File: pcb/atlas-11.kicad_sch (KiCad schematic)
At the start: 5 parts, among them J1 USB_C_Receptacle, J2 DCJ-11 SBC Expansion Bus, J3 Micro_SD_Card_Det2, U1 RP2350B-QFN80, U2 TPS22810DBVR

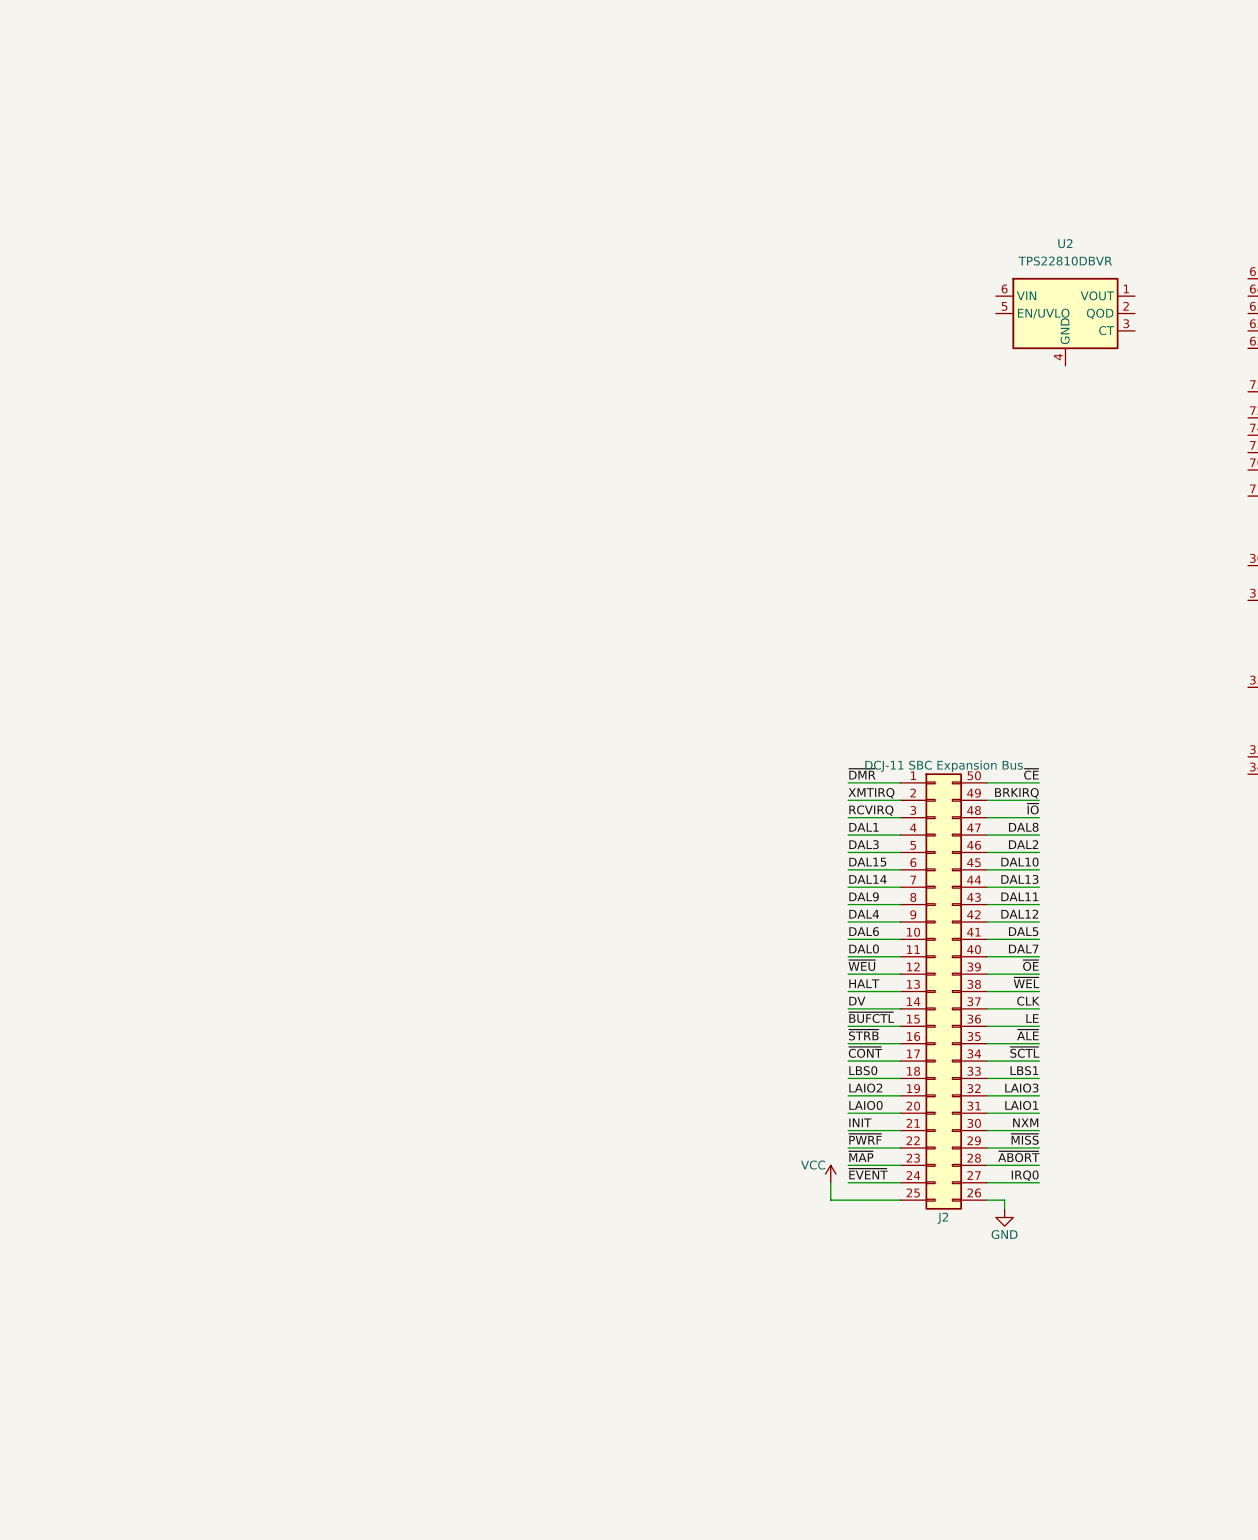
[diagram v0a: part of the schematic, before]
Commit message: add more sections from rp2350 minimal example
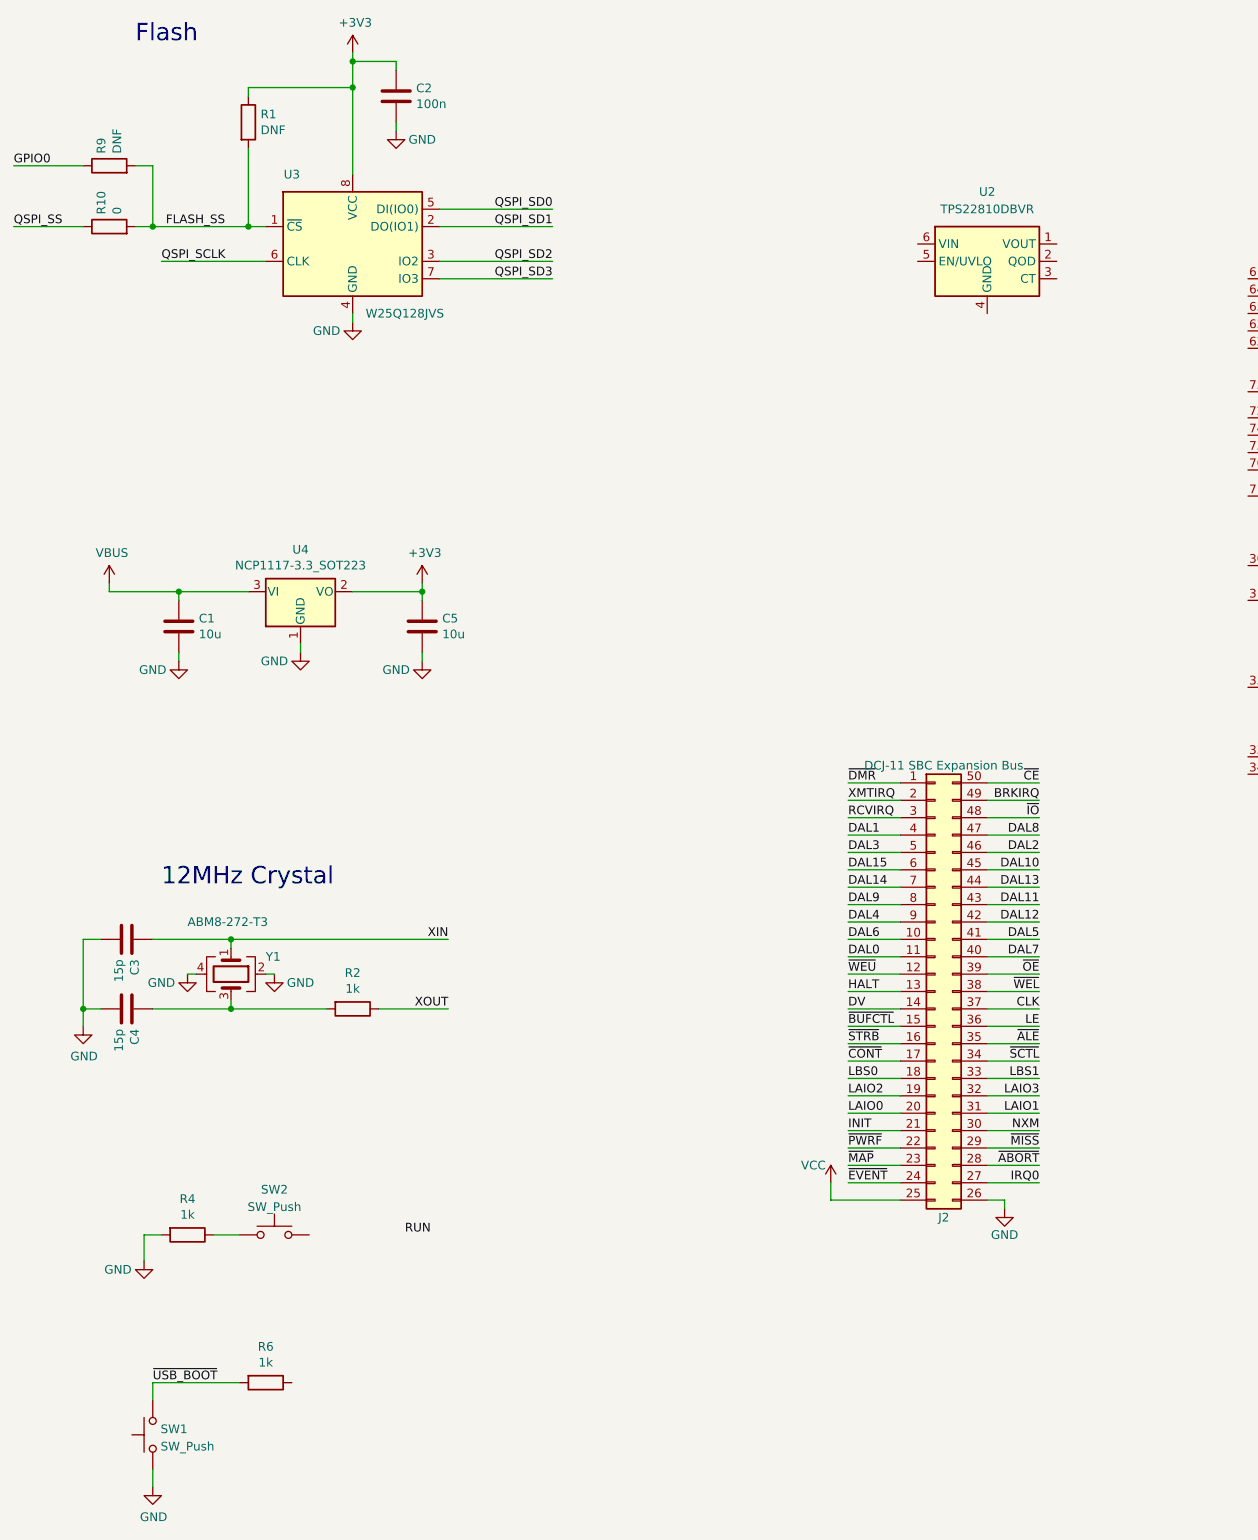
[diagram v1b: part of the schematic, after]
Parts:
- added C1, C5: 10u, Capacitor_SMD:C_0805_2012Metric, symbol Device:C
- added C2: 100n, Capacitor_SMD:C_0402_1005Metric, symbol Device:C
- added C3, C4: 15p, Capacitor_SMD:C_0402_1005Metric, symbol Device:C
- added R1, R9: DNF, Resistor_SMD:R_0402_1005Metric, symbol Device:R
- added R10: 0, Resistor_SMD:R_0402_1005Metric, symbol Device:R
- added R2, R4, R6: 1k, Resistor_SMD:R_0402_1005Metric, symbol Device:R
- added SW1, SW2: SW_Push, Button_Switch_SMD:SW_Push_1P1T_NO_Vertical_Wuerth_434133025816, symbol Switch:SW_Push
- added U3: W25Q128JVS, Package_SO:SOIC-8_5.23x5.23mm_P1.27mm, symbol Memory_Flash:W25Q128JVS
- added U4: NCP1117-3.3_SOT223, Package_TO_SOT_SMD:SOT-223-3_TabPin2, symbol Regulator_Linear:NCP1117-3.3_SOT223
- added Y1: ABM8-272-T3, Crystal:Crystal_SMD_3225-4Pin_3.2x2.5mm, symbol Device:Crystal_GND24
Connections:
- net GND: now also C1.2, C2.2, C3.2, C4.2, C5.2, R4.2, SW1.1, U3.4 (GND), U4.1 (GND), Y1.2, Y1.4
- new net: R4.1, SW2.1
- new net: C4.1, R2.2, Y1.3
- new net +3V3: C2.1, C5.1, R1.1, U3.8 (VCC), U4.2 (VO)
- new net FLASH_SS: R1.2, R10.2, R9.2, U3.1 (~{CS})
- new net GPIO0: R9.1
- new net QSPI_SCLK: U3.6 (CLK)
- new net QSPI_SD0: U3.5 (DI(IO0))
- new net QSPI_SD1: U3.2 (DO(IO1))
- new net QSPI_SD2: U3.3 (IO2)
- new net QSPI_SD3: U3.7 (IO3)
- new net QSPI_SS: R10.1
- new net VBUS: C1.1, U4.3 (VI)
- new net XIN: C3.1, Y1.1
- new net XOUT: R2.1
- new net ~{USB_BOOT}: R6.2, SW1.2
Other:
- note added: "12MHz Crystal"
- note added: "Flash"
- moved on the sheet: U2

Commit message: schematics & pcb work
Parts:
- removed R1, R9: DNF, Resistor_SMD:R_0402_1005Metric, symbol Device:R
- removed R10: 0, Resistor_SMD:R_0402_1005Metric, symbol Device:R
- added C10, C9: 4.7u, Capacitor_SMD:C_0402_1005Metric, symbol Device:C
- added C11, C12, C13, C14, C15, C16, C17, C18, C19, C20, C8: 100n, Capacitor_SMD:C_0402_1005Metric, symbol Device:C
- added C6, C7: 4.7u, RP2350_60QFN_minimal:C_0402_1005Metric_small_pads, symbol Device:C
- added J4: DCJ-11 SBC Bus Probe Interface, Library:DCJ-11 SBC Expansion Port Debug Header, symbol Connector_Generic:Conn_02x25_Counter_Clockwise
- added L1: 3.3u, RP2350_60QFN_minimal:L_pol_2016, symbol Device:L
- added R5: 33, Resistor_SMD:R_0402_1005Metric, symbol Device:R
- added R7, R8: 27, Resistor_SMD:R_0402_1005Metric, symbol Device:R
- J1: value USB_C_Receptacle -> USB
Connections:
- net FLASH_SS is gone; now on net QSPI_SS: U3.1 (~{CS})
- net VCC is gone; now on net SBC_POWER: J2.25 (Pin_25)
- net +3V3: now also U1.15 (IOVDD), U1.24 (IOVDD), U1.29 (IOVDD), U1.41 (IOVDD), U1.5 (IOVDD), U1.50 (IOVDD), U1.59 (ADC_AVDD), U1.60 (IOVDD), U1.64 (VREG_VIN), U1.68 (USB_OTP_VDD), U1.69 (QSPI_IOVDD), U1.76 (IOVDD), C12.1, C13.1, C14.1, C15.1, C16.1, C17.1, C18.1, C6.1, R5.1
- net BRKIRQ: now also J4.49 (Pin_49)
- net CLK: now also J4.37 (Pin_37)
- net DAL0: now also U1.2 (GPIO5), J4.11 (Pin_11)
- net DAL1: now also U1.3 (GPIO6), J4.4 (Pin_4)
- net DAL10: now also U1.14 (GPIO15), J4.45 (Pin_45)
- net DAL11: now also U1.16 (GPIO16), J4.43 (Pin_43)
- net DAL12: now also U1.17 (GPIO17), J4.42 (Pin_42)
- net DAL13: now also U1.18 (GPIO18), J4.44 (Pin_44)
- net DAL14: now also U1.19 (GPIO19), J4.7 (Pin_7)
- net DAL15: now also U1.20 (GPIO20), J4.6 (Pin_6)
- net DAL2: now also U1.4 (GPIO7), J4.46 (Pin_46)
- net DAL3: now also U1.6 (GPIO8), J4.5 (Pin_5)
- net DAL4: now also U1.7 (GPIO9), J4.9 (Pin_9)
- net DAL5: now also U1.8 (GPIO10), J4.41 (Pin_41)
- net DAL6: now also U1.9 (GPIO11), J4.10 (Pin_10)
- net DAL7: now also U1.11 (GPIO12), J4.40 (Pin_40)
- net DAL8: now also U1.12 (GPIO13), J4.47 (Pin_47)
- net DAL9: now also U1.13 (GPIO14), J4.8 (Pin_8)
- net DV: now also J4.14 (Pin_14)
- net GND: now also U1.62 (VREG_PGND), U2.4 (GND), U2.7 (GND), C10.2, C11.2, C12.2, C13.2, C14.2, C15.2, C16.2, C17.2, C18.2, C19.2, C20.2, C6.2, C7.2, C8.2, C9.2, J4.26 (Pin_26)
- net HALT: now also J4.13 (Pin_13)
- net INIT: now also J4.21 (Pin_21)
- net IRQ0: now also J4.27 (Pin_27)
- net LAIO0: now also J4.20 (Pin_20)
- net LAIO1: now also J4.31 (Pin_31)
- net LAIO2: now also J4.19 (Pin_19)
- net LAIO3: now also J4.32 (Pin_32)
- net LBS0: now also J4.18 (Pin_18)
- net LBS1: now also J4.33 (Pin_33)
- net LE: now also J4.36 (Pin_36)
- net NXM: now also J4.30 (Pin_30)
- net QSPI_SCLK: now also U1.71 (QSPI_SCLK)
- net QSPI_SD0: now also U1.72 (QSPI_SD0)
- net QSPI_SD1: now also U1.74 (QSPI_SD1)
- net QSPI_SD2: now also U1.73 (QSPI_SD2)
- net QSPI_SD3: now also U1.70 (QSPI_SD3)
- net QSPI_SS: now also R6.1, U1.75 (QSPI_SS)
- net RCVIRQ: now also J4.3 (Pin_3)
- net VBUS: now also U2.6 (VIN), C20.1
- net XIN: now also U1.30 (XIN)
- net XMTIRQ: now also J4.2 (Pin_2)
- net XOUT: now also U1.31 (XOUT)
- net ~{ABORT}: now also J4.28 (Pin_28)
- net ~{ALE}: now also J4.35 (Pin_35)
- net ~{BUFCTL}: now also J4.15 (Pin_15)
- net ~{CE}: now also J4.50 (Pin_50)
- net ~{CONT}: now also J4.17 (Pin_17)
- net ~{DMR}: now also J4.1 (Pin_1)
- net ~{EVENT}: now also J4.24 (Pin_24)
- net ~{IO}: now also J4.48 (Pin_48)
- net ~{MAP}: now also J4.23 (Pin_23)
- net ~{MISS}: now also J4.29 (Pin_29)
- net ~{OE}: now also J4.39 (Pin_39)
- net ~{PWRF}: now also J4.22 (Pin_22)
- net ~{SCTL}: now also J4.34 (Pin_34)
- net ~{STRB}: now also J4.16 (Pin_16)
- net ~{WEL}: now also J4.38 (Pin_38)
- net ~{WEU}: now also J4.12 (Pin_12)
- net at SW2.2: now also U1.35 (RUN)
- net SBC_POWER: now reaches U2.1 (VOUT)
- net SBC_POWER: now also C19.1, J4.25 (Pin_25)
- net SBC_ON: now reaches U2.5 (EN/UVLO)
- net SBC_ON: now also U1.79 (GPIO2)
- net +1V1: now reaches U1.10 (DVDD)
- net +1V1: now also U1.32 (DVDD), U1.51 (DVDD), U1.65 (VREG_FB), C10.1, C11.1, C7.1, C8.1, L1.1
- net VREG_AVDD: now reaches U1.61 (VREG_AVDD)
- net VREG_AVDD: now also C9.1, R5.2
- net VREG_LX: now reaches U1.63 (VREG_LX)
- net VREG_LX: now also L1.2
- net at U1.66 (USB_DM): now also R8.2
- net at U1.67 (USB_DP): now also R7.2
- new net USB_D+: R7.1
- new net USB_D-: R8.1
- no-connect marks 0 -> 2
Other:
- note added: "Make sure R7 and R8 are close to RP2350"
- title: (none) -> ATLAS-11
- moved on the sheet: C1, C2, C3, C4, C5, J1, J2, J3, R2, R4, R6, SW1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

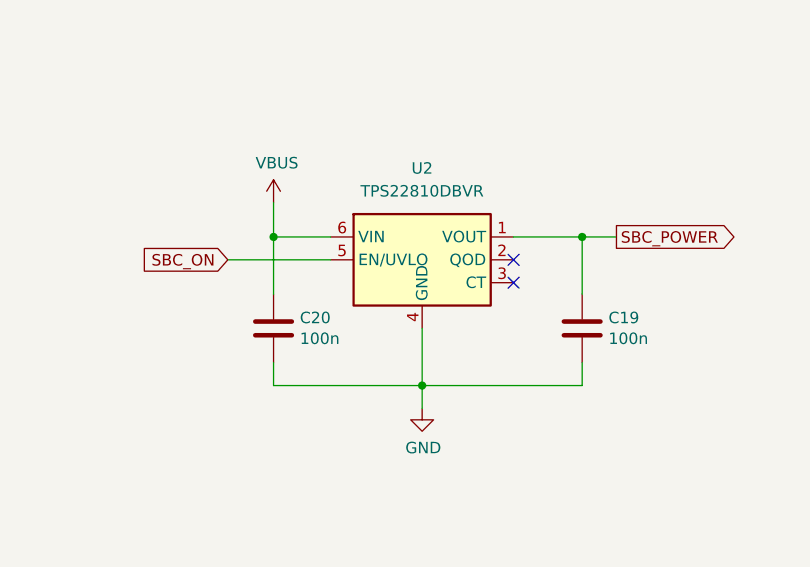
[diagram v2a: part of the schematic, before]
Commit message: fix tps22810 pinout
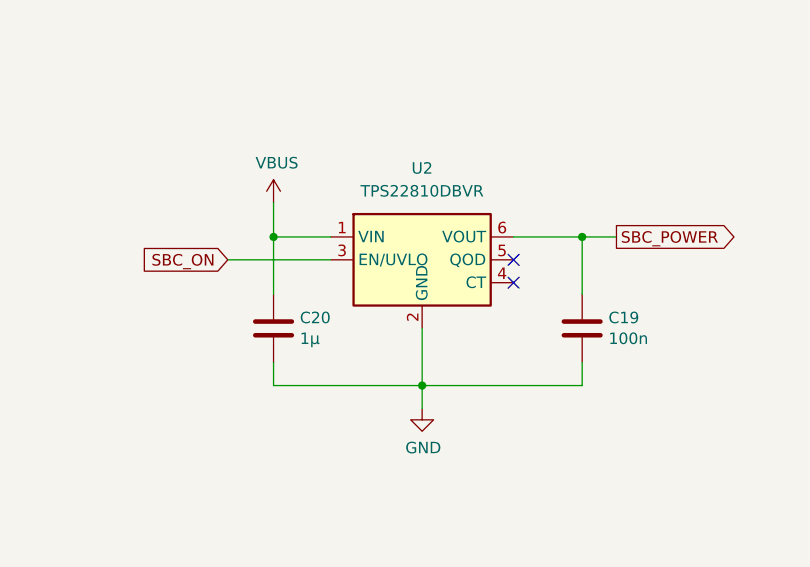
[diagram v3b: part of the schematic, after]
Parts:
- C20: value 100n -> 1µ
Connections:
- net GND: now also U2.2 (GND); no longer U2.4 (GND)
- net SBC_ON: now also U2.3 (EN/UVLO); no longer U2.5 (EN/UVLO)
- net SBC_POWER: now also U2.6 (VOUT); no longer U2.1 (VOUT)
- net VBUS: now also U2.1 (VIN); no longer U2.6 (VIN)
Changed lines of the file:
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@@
 			)
 		)
-		(property "Value" "100n"
+		(property "Value" "1µ"
 			(at 121.031 218.313 0)
 			(effects

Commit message: pcb work
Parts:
- removed J1: USB, Connector_USB:USB_C_Receptacle_Amphenol_12401948E412A, symbol Connector:USB_C_Receptacle
- removed J3: Micro_SD_Card_Det2, Connector_Card:microSD_HC_Molex_104031-0811, symbol Connector:Micro_SD_Card_Det2
- added J1: Micro_SD_Card_Det1, Connector_Card:microSD_HC_Hirose_DM3BT-DSF-PEJS, symbol Connector:Micro_SD_Card_Det1
- added J3: SWD, symbol Connector_Generic:Conn_01x03
- added J5: UART0, symbol Connector_Generic:Conn_01x03
- added P1: USB, Connector_USB:USB_C_Receptacle_G-Switch_GT-USB-7010ASV, symbol Connector:USB_C_Plug_USB2.0
- C17: footprint Capacitor_SMD:C_0402_1005Metric -> Capacitor_SMD:C_0603_1608Metric_Pad1.08x0.95mm_HandSolder
- SW1: value SW_Push -> USB BOOT
- SW2: value SW_Push -> RUN
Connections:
- net +3V3: now also J1.4 (VDD)
- net GND: now also SW2.1, U1.81 (GND), J1.6 (VSS), J3.2 (Pin_2), J5.2 (Pin_2); no longer R4.2
- net HALT: now also U1.22 (GPIO22)
- net INIT: now also U1.27 (GPIO26)
- net ~{ALE}: now also U1.23 (GPIO23)
- net ~{BUFCTL}: now also U1.21 (GPIO21)
- net ~{CONT}: now also U1.26 (GPIO25)
- net ~{IO}: now also U1.28 (GPIO27)
- net ~{SCTL}: now also U1.25 (GPIO24)
- net at R4.1: now also U1.35 (RUN); no longer SW2.1
- net at SW2.2: now also R4.2; no longer U1.35 (RUN)
- net SWCLK: now reaches U1.33 (SWCLK)
- net SWCLK: now also J3.3 (Pin_3)
- net SWDIO: now reaches U1.34 (SWDIO)
- net SWDIO: now also J3.1 (Pin_1)
- net SDCARD_DET: now reaches U1.53 (GPIO42_ADC2)
- net SDCARD_DET: now also J1.9 (DET)
- net SDCARD_MOSI: now reaches U1.54 (GPIO43_ADC3)
- net SDCARD_MOSI: now also J1.3 (CMD)
- net SDCARD_MISO: now reaches U1.55 (GPIO44_ADC4)
- net SDCARD_MISO: now also J1.7 (DAT0)
- net SDCARD_CS: now reaches U1.56 (GPIO45_ADC5)
- net SDCARD_CS: now also J1.2 (DAT3/CD)
- net SDCARD_CLK: now reaches U1.57 (GPIO46_ADC6)
- net SDCARD_CLK: now also J1.5 (CLK)
- net UART0_TX: now reaches U1.77 (GPIO0)
- net UART0_TX: now also J5.3 (Pin_3)
- net UART0_RX: now reaches U1.78 (GPIO1)
- net UART0_RX: now also J5.1 (Pin_1)
- net ~{USB_BOOT}: no longer names the net of R6.2, SW1.2
- new net: P1.A1 (GND), P1.A12 (GND), P1.B1 (GND), P1.B12 (GND)
- new net: P1.A4 (VBUS), P1.A9 (VBUS), P1.B4 (VBUS), P1.B9 (VBUS)
- no-connect marks 2 -> 4
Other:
- moved on the sheet: C2, R4, R6, SW1, SW2, U3

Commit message: pcb work
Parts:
- removed C6: 4.7u, RP2350_60QFN_minimal:C_0402_1005Metric_small_pads, symbol Device:C
- added C21: 4.7µ, Capacitor_SMD:C_0603_1608Metric_Pad1.08x0.95mm_HandSolder, symbol Device:C
- added D1: WS2812B, LED_SMD:LED_WS2812B_PLCC4_5.0x5.0mm_P3.2mm, symbol LED:WS2812B
- added D2, D3, D4: LED, symbol Device:LED
- added J6: WS2812 out, Connector_PinHeader_2.54mm:PinHeader_1x02_P2.54mm_Vertical, symbol Connector_Generic:Conn_01x02
- added R10: 150, Resistor_SMD:R_0402_1005Metric, symbol Device:R
- added R11, R9: 330, Resistor_SMD:R_0402_1005Metric, symbol Device:R
- added R12, R13: 1k, Resistor_SMD:R_0402_1005Metric, symbol Device:R
- added U5: MCP23017, Package_SO:SOIC-28W_7.5x17.9mm_P1.27mm, symbol Interface_Expansion:MCP23017_SO
- C7: value 4.7u -> 4.7µ; footprint RP2350_60QFN_minimal:C_0402_1005Metric_small_pads -> Capacitor_SMD:C_0603_1608Metric_Pad1.08x0.95mm_HandSolder
- C9: value 4.7u -> 4.7µ; footprint Capacitor_SMD:C_0402_1005Metric -> Capacitor_SMD:C_0603_1608Metric_Pad1.08x0.95mm_HandSolder
- J1: value Micro_SD_Card_Det1 -> SD Card
- J3: footprint (none) -> Connector_PinHeader_2.54mm:PinHeader_1x03_P2.54mm_Horizontal
- J5: footprint (none) -> Connector_PinSocket_2.54mm:PinSocket_1x03_P2.54mm_Horizontal
- L1: value 3.3u -> 3.3µ; footprint RP2350_60QFN_minimal:L_pol_2016 -> Inductor_SMD:L_0805_2012Metric_Pad1.15x1.40mm_HandSolder
- SW1: value USB BOOT -> BOOTSEL
- U1: value RP2350B-QFN80 -> RP2350B
- U3: footprint Package_SO:SOIC-8_5.23x5.23mm_P1.27mm -> Package_SO:SOIC-8_5.3x5.3mm_P1.27mm
- U4: value NCP1117-3.3_SOT223 -> NCP1117-3.3
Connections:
- net +3V3: now also C21.1, D3.2 (A), R12.1, R13.1, U5.9 (VDD)
- net GND: now also C21.2, D1.3 (VSS), J6.2 (Pin_2), R10.2, R11.2, R9.2, U5.10 (VSS), U5.15 (A0), U5.16 (A1), U5.17 (A2)
- net SBC_POWER: now also D2.2 (A)
- net VBUS: now also D1.1 (VDD), D4.2 (A)
- net LED1: now reaches U1.1 (GPIO4)
- net GPIO28: now reaches U1.36 (GPIO28)
- net GPIO29: now reaches U1.37 (GPIO29)
- net GPIO30: now reaches U1.38 (GPIO30)
- net GPIO31: now reaches U1.39 (GPIO31)
- net GPIO32: now reaches U1.40 (GPIO32)
- net GPIO33: now reaches U1.42 (GPIO33)
- net GPIO34: now reaches U1.43 (GPIO34)
- net GPIO35: now reaches U1.44 (GPIO35)
- net SINTA: now reaches U1.45 (GPIO36)
- net SINTB: now reaches U1.46 (GPIO37)
- net UINTA: now reaches U1.47 (GPIO38)
- net UINTA: now also U5.20 (INTA)
- net UINTB: now reaches U1.48 (GPIO39)
- net UINTB: now also U5.19 (INTB)
- net SDA: now reaches U1.49 (GPIO40_ADC0)
- net SDA: now also R12.2, U5.13 (SDA)
- net SCL: now reaches U1.52 (GPIO41_ADC1)
- net SCL: now also R13.2, U5.12 (SCK)
- net GPIO47: now reaches U1.58 (GPIO47_ADC7)
- net GPIO47: now also D1.4 (DIN)
- net LED0: now reaches U1.80 (GPIO3)
- new net: D3.1 (K), R10.1
- new net: D2.1 (K), R9.1
- new net: D4.1 (K), R11.1
- new net: D1.2 (DOUT), J6.1 (Pin_1)
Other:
- moved on the sheet: C19, C2, C20, C3, C4, J3, J5, R2, R4, R6, SW1, SW2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
